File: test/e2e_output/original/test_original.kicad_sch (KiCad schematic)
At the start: 3 parts, among them U1 CP_Radial_D25.0mm_P10.00mm_Sn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, U2 R_Axial_DIN0207_L6.3mm_D2.5mm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, U3 R_Axial_DIN0207_L6.3mm_D2.5mm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

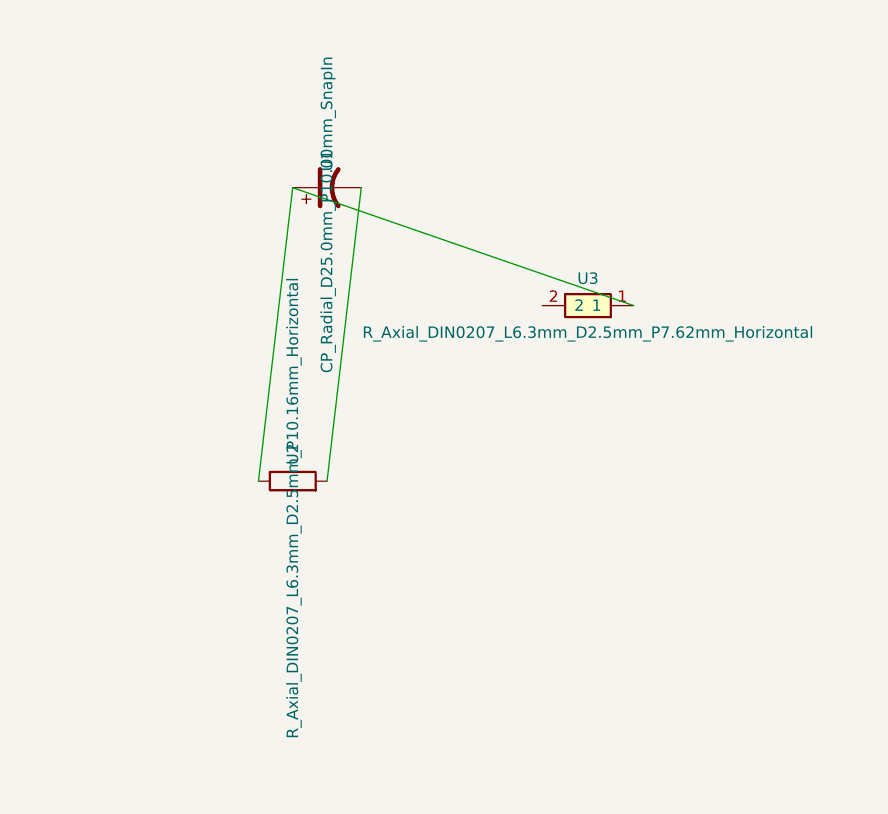
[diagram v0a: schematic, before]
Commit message: fix: schematic router - pin_map mapping + rotation formula alignment
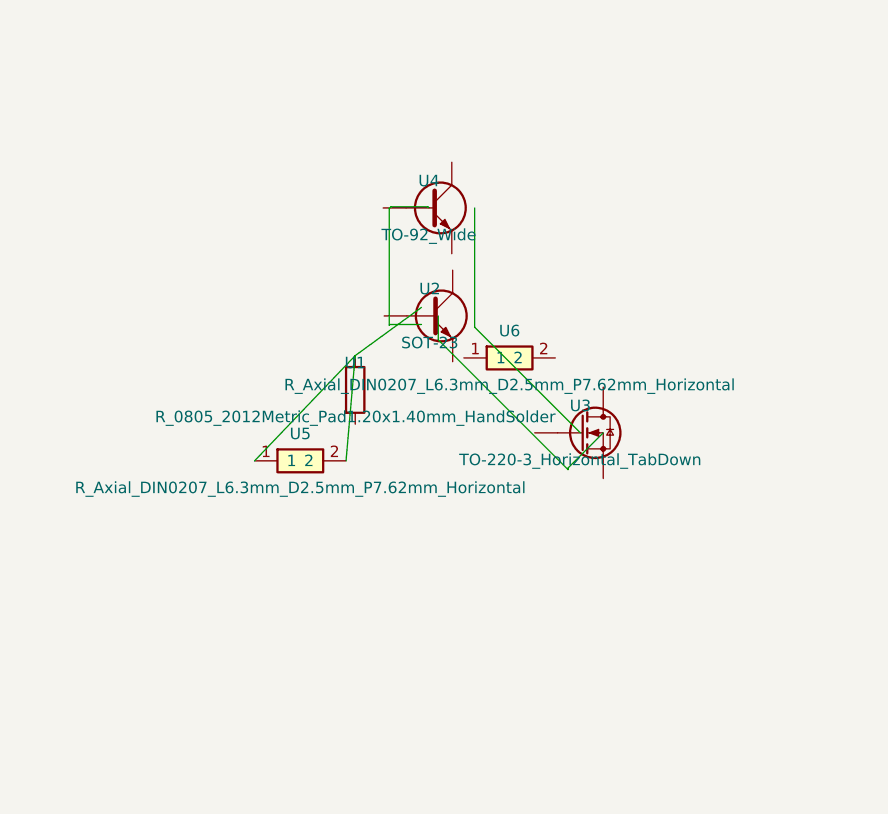
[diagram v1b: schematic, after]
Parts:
- removed U1: CP_Radial_D25.0mm_P10.00mm_SnapIn, 00_basic:CP_Radial_D25.0mm_P10.00mm_SnapIn, symbol 00_basic:C_Polarized
- removed U2: R_Axial_DIN0207_L6.3mm_D2.5mm_P10.16mm_Horizontal, 00_basic:R_Axial_DIN0207_L6.3mm_D2.5mm_P10.16mm_Horizontal, symbol 00_basic:R
- removed U3: R_Axial_DIN0207_L6.3mm_D2.5mm_P7.62mm_Horizontal, 00_basic:R_Axial_DIN0207_L6.3mm_D2.5mm_P7.62mm_Horizontal, symbol _placeholder:U3
- added U1: R_0805_2012Metric_Pad1.20x1.40mm_HandSolder, 00_basic:R_0805_2012Metric_Pad1.20x1.40mm_HandSolder, symbol RE_passive:R
- added U2: SOT-23, RE_active:SOT-23, symbol RE_active:Q_NPN
- added U3: TO-220-3_Horizontal_TabDown, RE_active:TO-220-3_Horizontal_TabDown, symbol RE_active:Q_NMOS
- added U4: TO-92_Wide, RE_active:TO-92_Wide, symbol RE_active:Q_NPN
- added U5: R_Axial_DIN0207_L6.3mm_D2.5mm_P7.62mm_Horizontal, RE_passive_tht:R_Axial_DIN0207_L6.3mm_D2.5mm_P7.62mm_Horizontal, symbol _placeholder:U5
- added U6: R_Axial_DIN0207_L6.3mm_D2.5mm_P7.62mm_Horizontal, RE_passive_tht:R_Axial_DIN0207_L6.3mm_D2.5mm_P7.62mm_Horizontal, symbol _placeholder:U6
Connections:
- new net: U1.1, U5.1, U5.2
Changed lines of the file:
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@@
   (paper "A4")
   (symbol
-    (lib_id "00_basic:C_Polarized")
-    (at 135.90 88.70 90)
-    (unit 1)
-    (exclude_from_sim no)
-    (in_bom yes)
-    (on_board yes)
-    (dnp no)
-    (property "Reference" "U1" (at 135.90 85.70 0)
-      (effects (font (size 1.27 1.27)))
-    )
-    (property "Value" "CP_Radial_D25.0mm_P10.00mm_SnapIn" (at 135.90 91.70 0)
-      (effects (font (size 1.27 1.27)))
-    )
-    (property "Footprint" "00_basic:CP_Radial_D25.0mm_P10.00mm_SnapIn" (at 135.90 93.70 0)
+    (lib_id "RE_passive:R")
+    (at 139.04 111.17 0)
+    (unit 1)
+    (exclude_from_sim no)
+    (in_bom yes)
+    (on_board yes)
+    (dnp no)
+    (property "Reference" "U1" (at 139.04 108.17 0)
+      (effects (font (size 1.27 1.27)))
+    )
+    (property "Value" "R_0805_2012Metric_Pad1.20x1.40mm_HandSolder" (at 139.04 114.17 0)
+      (effects (font (size 1.27 1.27)))
+    )
+    (property "Footprint" "00_basic:R_0805_2012Metric_Pad1.20x1.40mm_HandSolder" (at 139.04 116.17 0)
       (effects (font (size 1.27 1.27)) hide)
     )
@@
   )
   (symbol
-    (lib_id "00_basic:R")
-    (at 132.10 121.30 90)
-    (unit 1)
-    (exclude_from_sim no)
-    (in_bom yes)
-    (on_board yes)
-    (dnp no)
-    (property "Reference" "U2" (at 132.10 118.30 0)
-      (effects (font (size 1.27 1.27)))
-    )
-    (property "Value" "R_Axial_DIN0207_L6.3mm_D2.5mm_P10.16mm_Horizontal" (at 132.10 124.30 0)
-      (effects (font (size 1.27 1.27)))
-    )
-    (property "Footprint" "00_basic:R_Axial_DIN0207_L6.3mm_D2.5mm_P10.16mm_Horizontal" (at 132.10 126.30 0)
+    (lib_id "RE_active:Q_NPN")
+    (at 147.33 102.95 0)
+    (unit 1)
+    (exclude_from_sim no)
+    (in_bom yes)
+    (on_board yes)
+    (dnp no)
+    (property "Reference" "U2" (at 147.33 99.95 0)
+      (effects (font (size 1.27 1.27)))
+    )
+    (property "Value" "SOT-23" (at 147.33 105.95 0)
+      (effects (font (size 1.27 1.27)))
+    )
+    (property "Footprint" "RE_active:SOT-23" (at 147.33 107.95 0)
       (effects (font (size 1.27 1.27)) hide)
     )
@@
   )
   (symbol
-    (lib_id "_placeholder:U3")
-    (at 164.90 101.80 180)
-    (unit 1)
-    (exclude_from_sim no)
-    (in_bom yes)
-    (on_board yes)
-    (dnp no)
-    (property "Reference" "U3" (at 164.90 98.80 0)
-      (effects (font (size 1.27 1.27)))
-    )
-    (property "Value" "R_Axial_DIN0207_L6.3mm_D2.5mm_P7.62mm_Horizontal" (at 164.90 104.80 0)
-      (effects (font (size 1.27 1.27)))
-    )
-    (property "Footprint" "00_basic:R_Axial_DIN0207_L6.3mm_D2.5mm_P7.62mm_Horizontal" (at 164.90 106.80 0)
+    (lib_id "RE_active:Q_NMOS")
+    (at 164.06 115.94 0)
+    (unit 1)
+    (exclude_from_sim no)
+    (in_bom yes)
+    (on_board yes)
+    (dnp no)
+    (property "Reference" "U3" (at 164.06 112.94 0)
+      (effects (font (size 1.27 1.27)))
+    )
+    (property "Value" "TO-220-3_Horizontal_TabDown" (at 164.06 118.94 0)
+      (effects (font (size 1.27 1.27)))
+    )
+    (property "Footprint" "RE_active:TO-220-3_Horizontal_TabDown" (at 164.06 120.94 0)
       (effects (font (size 1.27 1.27)) hide)
     )
@@
     )
   )
-  (wire (pts (xy 128.29 121.30) (xy 132.09 88.70))
-    (stroke (width 0) (type default))
-  )
-  (wire (pts (xy 135.91 121.30) (xy 139.71 88.70))
-    (stroke (width 0) (type default))
-  )
-  (wire (pts (xy 132.09 88.70) (xy 169.98 101.80))
-    (stroke (width 0) (type default))
-  )
+  (symbol
+    (lib_id "RE_active:Q_NPN")
+    (at 147.23 90.95 0)
+    (unit 1)
+    (exclude_from_sim no)
+    (in_bom yes)
+    (on_board yes)
+    (dnp no)
+    (property "Reference" "U4" (at 147.23 87.95 0)
+      (effects (font (size 1.27 1.27)))
+    )
+    (property "Value" "TO-92_Wide" (at 147.23 93.95 0)
+      (effects (font (size 1.27 1.27)))
+    )
+    (property "Footprint" "RE_active:TO-92_Wide" (at 147.23 95.95 0)
+      (effects (font (size 1.27 1.27)) hide)
+    )
+    (instances
+      (project ""
+        (path "/"
+          (reference "U4")
+          (unit 1)
+        )
+      )
+    )
+  )
+  (symbol
+    (lib_id "_placeholder:U5")
+    (at 132.94 119.05 0)
+    (unit 1)
+    (exclude_from_sim no)
+    (in_bom yes)
+    (on_board yes)
+    (dnp no)
+    (property "Reference" "U5" (at 132.94 116.05 0)
+      (effects (font (size 1.27 1.27)))
+    )
+    (property "Value" "R_Axial_DIN0207_L6.3mm_D2.5mm_P7.62mm_Horizontal" (at 132.94 122.05 0)
+      (effects (font (size 1.27 1.27)))
+    )
+    (property "Footprint" "RE_passive_tht:R_Axial_DIN0207_L6.3mm_D2.5mm_P7.62mm_Horizontal" (at 132.94 124.05 0)
+      (effects (font (size 1.27 1.27)) hide)
+    )
+    (instances
+      (project ""
+        (path "/"
+          (reference "U5")
+          (unit 1)
+        )
+      )
+    )
+  )
+  (symbol
+    (lib_id "_placeholder:U6")
+    (at 156.19 107.62 0)
+    (unit 1)
+    (exclude_from_sim no)
+    (in_bom yes)
+    (on_board yes)
+    (dnp no)
+    (property "Reference" "U6" (at 156.19 104.62 0)
+      (effects (font (size 1.27 1.27)))
+    )
+    (property "Value" "R_Axial_DIN0207_L6.3mm_D2.5mm_P7.62mm_Horizontal" (at 156.19 110.62 0)
+      (effects (font (size 1.27 1.27)))
+    )
+    (property "Footprint" "RE_passive_tht:R_Axial_DIN0207_L6.3mm_D2.5mm_P7.62mm_Horizontal" (at 156.19 112.62 0)
+      (effects (font (size 1.27 1.27)) hide)
+    )
+    (instances
+      (project ""
+        (path "/"
+          (reference "U6")
+          (unit 1)
+        )
+      )
+    )
+  )
+  (wire (pts (xy 152.31 90.95) (xy 152.31 104.20))
+    (stroke (width 0) (type default))
+  )
+  (wire (pts (xy 152.31 104.20) (xy 164.06 115.94))
+    (stroke (width 0) (type default))
+  )
+  (wire (pts (xy 148.27 102.95) (xy 148.27 105.61))
+    (stroke (width 0) (type default))
+  )
+  (wire (pts (xy 148.27 105.61) (xy 162.68 120.02))
+    (stroke (width 0) (type default))
+  )
+  (wire (pts (xy 162.68 120.02) (xy 162.68 119.86))
+    (stroke (width 0) (type default))
+  )
+  (wire (pts (xy 162.68 119.86) (xy 166.60 115.94))
+    (stroke (width 0) (type default))
+  )
+  (wire (pts (xy 146.40 103.90) (xy 142.90 103.90))
+    (stroke (width 0) (type default))
+  )
+  (wire (pts (xy 142.90 103.90) (xy 142.82 103.97))
+    (stroke (width 0) (type default))
+  )
+  (wire (pts (xy 142.82 103.97) (xy 142.82 91.02))
+    (stroke (width 0) (type default))
+  )
+  (wire (pts (xy 142.82 91.02) (xy 143.02 90.82))
+    (stroke (width 0) (type default))
+  )
+  (wire (pts (xy 143.02 90.82) (xy 147.10 90.82))
+    (stroke (width 0) (type default))
+  )
+  (wire (pts (xy 147.10 90.82) (xy 147.23 90.95))
+    (stroke (width 0) (type default))
+  )
+  (wire (pts (xy 139.04 107.36) (xy 146.40 102.00))
+    (stroke (width 0) (type default))
+  )
+  (wire (pts (xy 139.04 107.36) (xy 127.86 119.05))
+    (stroke (width 0) (type default))
+  )
+  (wire (pts (xy 139.04 107.36) (xy 138.02 119.05))
+    (stroke (width 0) (type default))
+  )

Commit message: backup
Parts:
- added U7: CP_Radial_D30.0mm_P10.00mm_SnapIn, RE_passive_tht:CP_Radial_D30.0mm_P10.00mm_SnapIn, symbol RE_passive:C_Polarized
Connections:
- net at U1.1, U5.1, U5.2: now also U2.C, U3.D, U4.B, U4.C
- net at U3.G: now also U7.2
